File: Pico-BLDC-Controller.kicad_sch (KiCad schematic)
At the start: 150 parts, among them J1 Conn_01x10, J2 Heat Mat, J3 I2C CONN, J4 USB_C_Receptacle_USB2.0_14P, J5 SM03B-SRSS-TB, J6 Conn_01x05, J7 Conn_01x02, J8 Conn_01x03, Q1 DMN3053L-7, Q2 SIR680LDP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

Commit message: all
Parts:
- removed H1, H2, H3, H4: MountingHole, MountingHole:MountingHole_2.7mm_M2.5_ISO14580, symbol Mechanical:MountingHole
- added H1, H2, H3, H4: MountingHole_Pad, MountingHole:MountingHole_2.2mm_M2_DIN965_Pad_TopBottom, symbol Mechanical:MountingHole_Pad
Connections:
- net GND: now also H1.1, H2.1, H3.1, H4.1

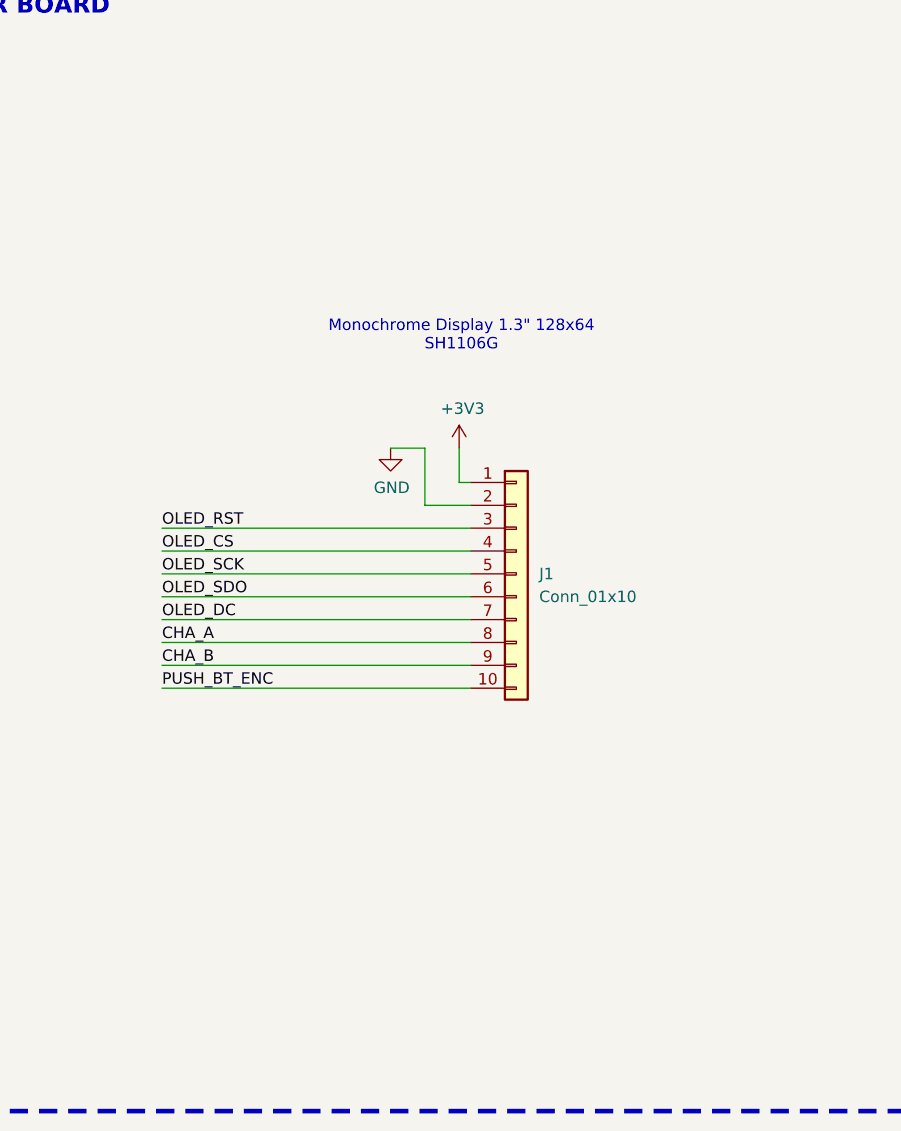
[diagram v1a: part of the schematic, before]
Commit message: change connector to usb-c
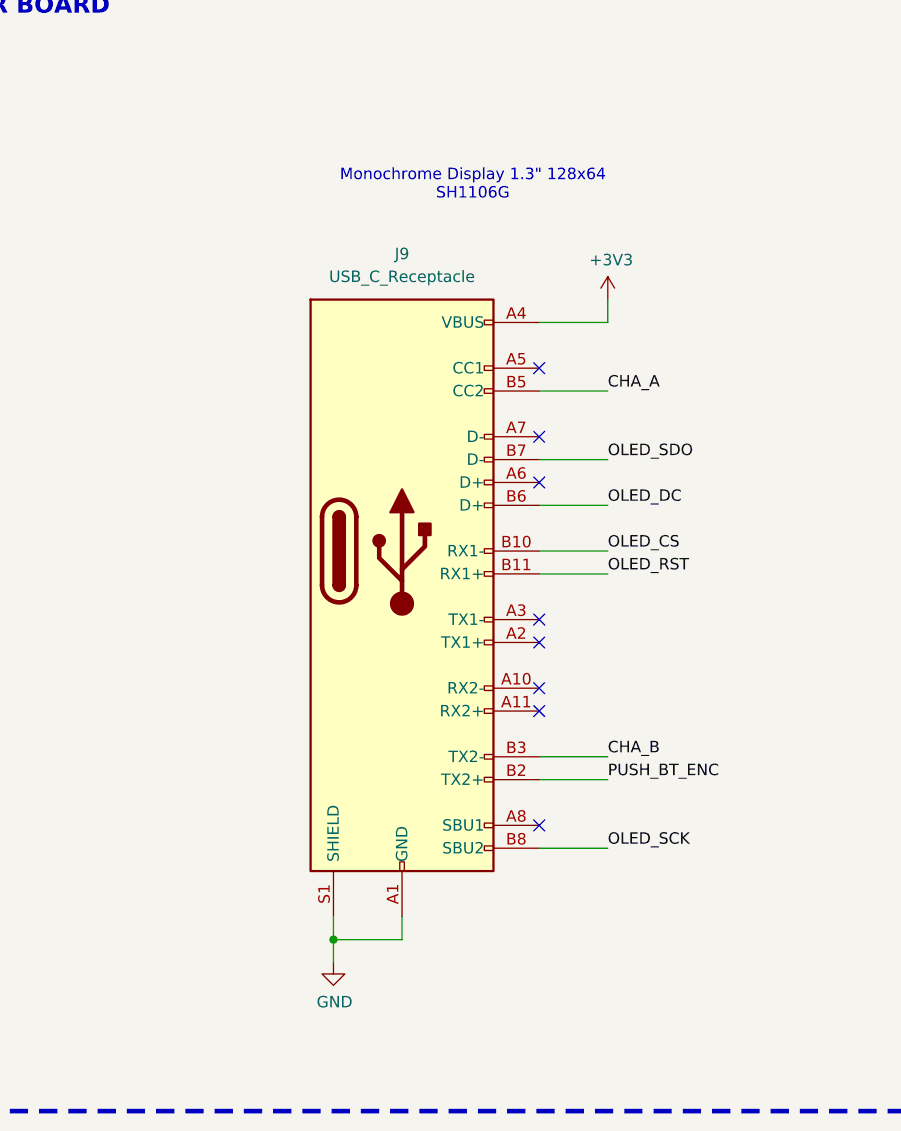
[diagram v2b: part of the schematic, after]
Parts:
- removed J1: Conn_01x10, Connector_JST:JST_PHD_B10B-PHDSS_2x05_P2.00mm_Vertical, symbol Connector_Generic:Conn_01x10
- added J9: USB_C_Receptacle, Connector_USB:USB_C_Receptacle_JAE_DX07S024WJ3R400, symbol Connector:USB_C_Receptacle
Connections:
- net +3V3: now also J9.A4 (VBUS), J9.A9 (VBUS), J9.B4 (VBUS), J9.B9 (VBUS)
- net CHA_A: now also J9.B5 (CC2)
- net CHA_B: now also J9.B3 (TX2-)
- net GND: now also J9.A1 (GND), J9.A12 (GND), J9.B1 (GND), J9.B12 (GND), J9.S1 (SHIELD)
- net GPIO0: now also J9.B11 (RX1+)
- net GPIO1: now also J9.B10 (RX1-)
- net GPIO2: now also J9.B8 (SBU2)
- net GPIO3: now also J9.B7 (D-)
- net GPIO4: now also J9.B6 (D+)
- net GPIO7: now also J9.B2 (TX2+)
- no-connect marks 0 -> 8
